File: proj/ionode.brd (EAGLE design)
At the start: 43.2 x 15.2 mm, 34 parts, among them J2 USB-BAMPHENOL-MICRO, U1 ATMEGA1284P-MU44-VQFN, U4 FT232RQFN32, U5 SN74LVC1G125SOT23-5, U6 SN74LVC1G125SOT23-5, U7 3.3V, X1 10MHz

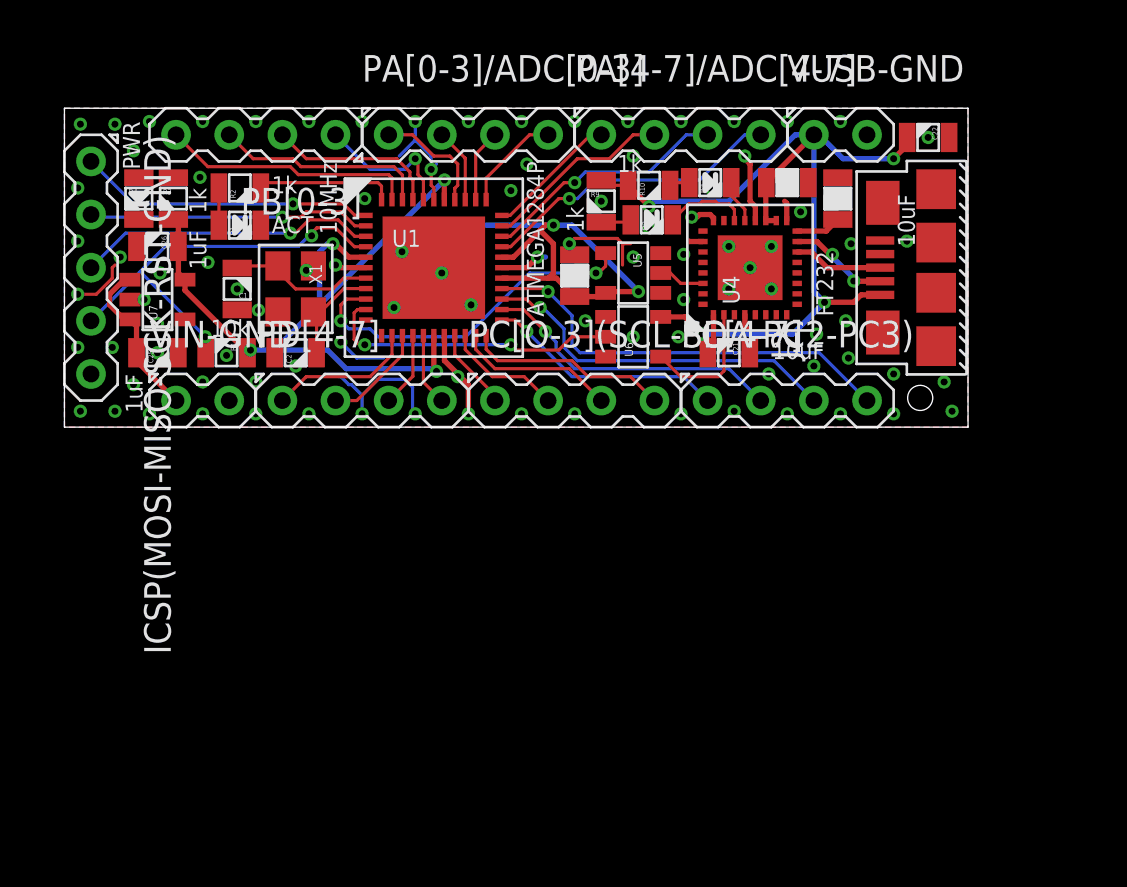
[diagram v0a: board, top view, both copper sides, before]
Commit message: Improved reference designators on ionode
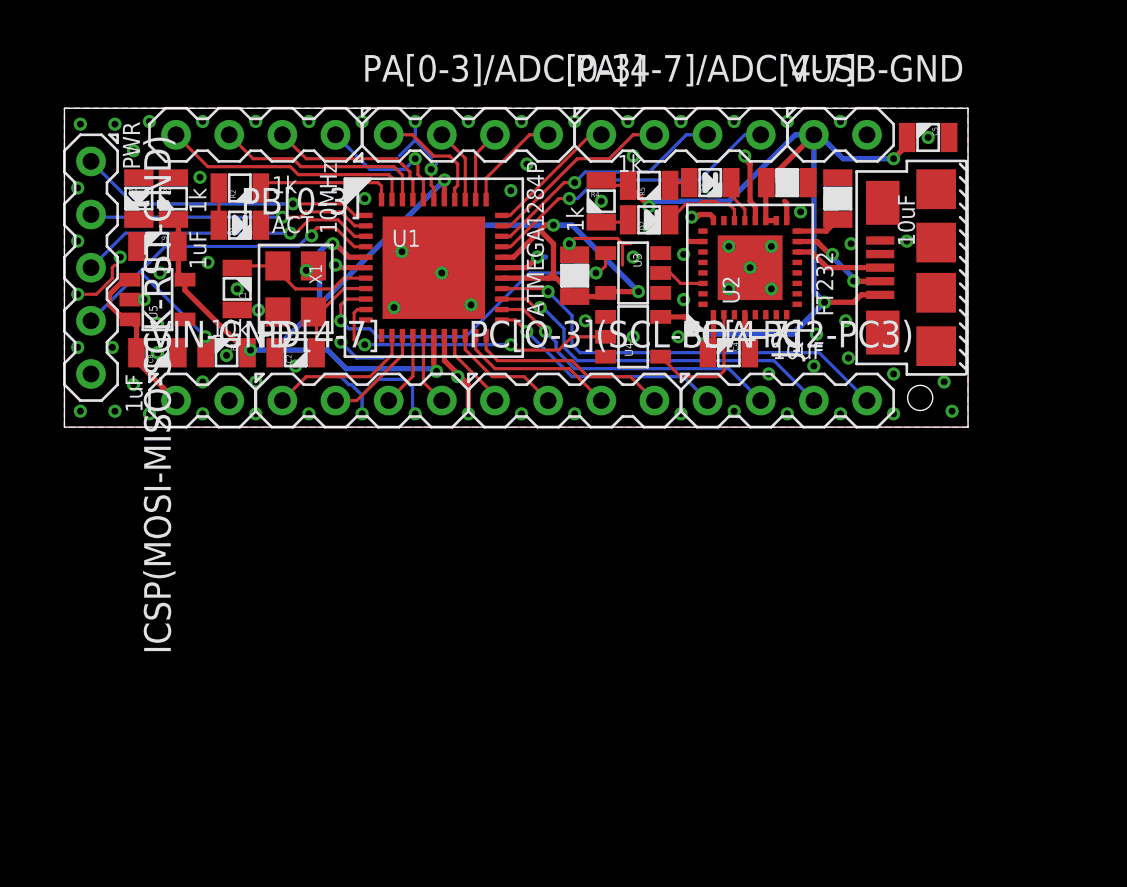
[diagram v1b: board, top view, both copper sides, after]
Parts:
- removed U6: SN74LVC1G125SOT23-5, dooba:SOT23-5
- removed U7: 3.3V, dooba:SOT23-5
- added U2: FT232RQFN32, dooba:32-VQFN
- added U3: SN74LVC1G125SOT23-5, dooba:SOT23-5
- U4: value FT232RQFN32 -> SN74LVC1G125SOT23-5; device dooba:32-VQFN -> dooba:SOT23-5
- U5: value SN74LVC1G125SOT23-5 -> 3.3V
- moved U5 22.8 mm to (28.3, 31.5), turned to 90 degrees
- moved U4 6.49 mm to (51.1, 29.7)
- moved D2 0.13 mm to (51.8, 35.3)
- renumbered C21 to C4, C22 to C5, C23 to C6, C24 to C7, C25 to C8, C26 to C9, R10 to R5, R9 to R4
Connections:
- net 3.3V: now also U3.5; no longer U7.5
- net ATMEGA_RX: now also U3.4; no longer U5.4
- net ATMEGA_TX: now also U4.2; no longer U6.2
- net FT232R_RX: now also U2.P$2, U4.4; no longer U4.P$2, U6.4
- net FT232R_TX: now also U2.P$30, U3.2; no longer U4.P$30, U5.2
- net GND: now also U2.P$17, U2.P$20, U2.P$24, U2.P$26, U2.P$33, U2.P$4, U3.1, U3.3, U4.1, U4.3, U5.2; no longer U4.P$17, U4.P$20, U4.P$24, U4.P$26, U4.P$33, U4.P$4, U5.1, U5.3, U6.1, U6.3, U7.2
- net N$21: now also U2.P$16; no longer U4.P$16
- net N$22: now also U2.P$22; no longer U4.P$22
- net N$23: now also U2.P$21; no longer U4.P$21
- net N$26: now also U2.P$15; no longer U4.P$15
- net N$27: now also U2.P$14; no longer U4.P$14
- net VIN: now also U5.1, U5.3; no longer U7.1, U7.3
- net VUSB: now also U2.P$1, U2.P$18, U2.P$19, U4.5; no longer U4.P$1, U4.P$18, U4.P$19, U6.5
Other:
- board text added: "C1"
- board text added: "C2"
- board text added: "C3"
- board text added: "C4"
- board text added: "C5"
- board text added: "C6"
- board text added: "C7"
- board text added: "C8"
- board text added: "C9"
- board text added: "D1"
- board text added: "D2"
- board text added: "D3"
- board text added: "D4"
- board text added: "J1"
- board text added: "R1"
- board text added: "R2"
- board text added: "R3"
- board text added: "R4"
- board text added: "R5"
- board text added: "U1"
- board text added: "U2"
- board text added: "U3"
- board text added: "U4"
- board text added: "U5"
- board text added: "X1"

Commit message: Added DRU file for ZhongFeng PCBA Added 0402 footprint Added SMD Jumper footprint Added SMD Jumper to ioNode for VIN - VUSB Upgraded most 0805 parts on ioNode to 0402 Added USART1 TX/RX breakout on ioNode Upgraded ioNode board to better use ZFPCBA DRU
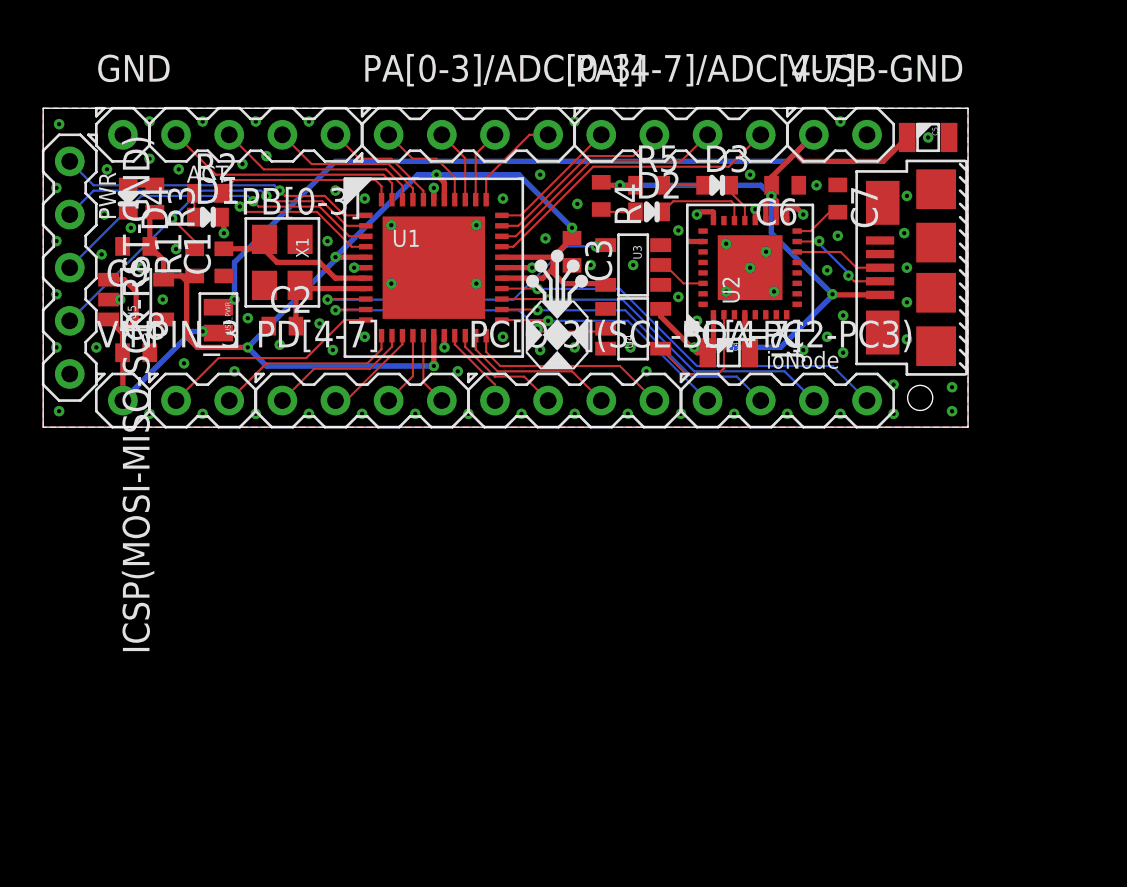
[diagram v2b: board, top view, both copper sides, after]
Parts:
- added GND, VIN: PIN_1, dooba:PIN_1
- added USB_PWR: JMPSMD, dooba:SMD_JMP
- C1, C2, C3, C6, C7, C8, C9, D1, D2, D3, D4, R1, R2, R3, R4, R5: device dooba:0805 -> dooba:0402
- PIN_3: value PIN_2 -> PD[2-3]
- moved R1 4.58 mm to (30.1, 33.3), turned to 90 degrees
- moved D1 1.57 mm to (30.7, 35.4)
- moved R2 1.55 mm to (30.7, 36.6)
- moved C1 1.42 mm to (31.5, 33.3)
- moved X1 1.42 mm to (34.3, 33.3)
- moved C2 1.42 mm to (34.3, 30.2)
- moved C3 1.15 mm to (48.1, 33.8), turned to 270 degrees
- moved C8 1.02 mm to (27.3, 29.0)
- moved C9 1.02 mm to (27.3, 34.0)
- moved ICSP(MOSI-MISO-SCK-RST-GND) 1.02 mm to (24.1, 33.0)
- moved U5 1.02 mm to (27.3, 31.5)
- moved R3 0.89 mm to (28.2, 36.3)
- moved D4 0.51 mm to (26.9, 36.3)
- moved D2 0.38 mm to (51.8, 35.7)
- moved U3 0.38 mm to (51.1, 33.1)
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- renumbered VIN-GND to PIN_3
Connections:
- net GND: now also GND.1; no longer PIN_3.2
- net PD2/RXD1: now also PIN_3.1
- net PD3/TXD1: now also PIN_3.2
- net VIN: now also USB_PWR.2, VIN.1; no longer PIN_3.1
- net VUSB: now also USB_PWR.1
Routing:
- net VUSB: track 46.0 -> 76.2 mm, vias 4 -> 5
- net GND: track 36.0 -> 11.3 mm, vias 97 -> 99
- net PD2/RXD1: track 0.00 -> 10.7 mm
- net PD3/TXD1: track 0.00 -> 8.94 mm
- net 3.3V: track 62.3 -> 55.5 mm, vias 6 -> 5
- net VIN: track 7.82 -> 13.9 mm, vias 0 -> 1
- net N$6: track 6.59 -> 8.68 mm
- net PB7/SCK: track 14.4 -> 16.4 mm
- net PB6/MISO: track 13.6 -> 15.3 mm
- net !RESET: track 20.6 -> 19.3 mm
- net PB0: track 6.82 -> 5.73 mm, vias 1 -> 0
- net N$2: track 7.01 -> 8.03 mm
- net PB5/MOSI: track 14.2 -> 15.2 mm
- net N$25: track 0.97 -> 1.95 mm
- net ATMEGA_RX: track 17.1 -> 16.2 mm
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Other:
- board size 43.2 x 15.2 mm -> 44.2 x 15.2 mm
- board text added: "ioNode"
- board text removed: "10MHz"
- board text removed: "10k"
- board text removed: "10uF"
- board text removed: "1k"
- board text removed: "1uF"
- board text removed: "ATMEGA1284P"
- board text removed: "C1"
- board text removed: "C2"
- board text removed: "C3"
- board text removed: "C6"
- board text removed: "C7"
- board text removed: "C8"
- board text removed: "C9"
- board text removed: "D1"
- board text removed: "D2"
- board text removed: "D3"
- board text removed: "D4"
- board text removed: "FT232"
- board text removed: "R1"
- board text removed: "R2"
- board text removed: "R3"
- board text removed: "R4"
- board text removed: "R5"

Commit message: Completed Tako Module
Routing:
- net GND: track 11.3 -> 13.0 mm
- net VUSB: track 76.2 -> 75.6 mm
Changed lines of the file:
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@@
 <wire x1="38.279" y1="33.02" x2="37.719" y2="33.02" width="0.254" layer="1"/>
 <via x="37.719" y="33.02" extent="1-16" drill="0.2032"/>
-<wire x1="54.392" y1="34.27" x2="53.741" y2="34.27" width="0.254" layer="1"/>
+<wire x1="54.192" y1="34.27" x2="53.741" y2="34.27" width="0.254" layer="1"/>
 <wire x1="53.741" y1="34.27" x2="53.721" y2="34.29" width="0.254" layer="1"/>
-<wire x1="54.892" y1="35.27" x2="54.892" y2="35.659" width="0.254" layer="1"/>
+<wire x1="54.892" y1="35.47" x2="54.892" y2="35.659" width="0.254" layer="1"/>
 <wire x1="54.892" y1="35.659" x2="54.864" y2="35.687" width="0.254" layer="1"/>
 <wire x1="54.864" y1="35.687" x2="54.229" y2="35.687" width="0.254" layer="1"/>
-<wire x1="56.892" y1="35.27" x2="56.892" y2="35.81" width="0.254" layer="1"/>
+<wire x1="56.892" y1="35.47" x2="56.892" y2="35.81" width="0.254" layer="1"/>
 <wire x1="56.892" y1="35.81" x2="56.896" y2="35.814" width="0.254" layer="1"/>
 <via x="56.896" y="35.814" extent="1-16" drill="0.2032"/>
-<wire x1="58.392" y1="35.27" x2="58.392" y2="35.786" width="0.254" layer="1"/>
-<wire x1="56.392" y1="30.77" x2="56.392" y2="30.103" width="0.254" layer="1"/>
+<wire x1="58.392" y1="35.47" x2="58.392" y2="35.786" width="0.254" layer="1"/>
+<wire x1="56.392" y1="30.57" x2="56.392" y2="30.103" width="0.254" layer="1"/>
 <wire x1="56.392" y1="30.103" x2="56.388" y2="30.099" width="0.254" layer="1"/>
 <via x="55.499" y="31.877" extent="1-16" drill="0.2032"/>
@@
 <wire x1="41.529" y1="33.02" x2="40.259" y2="33.02" width="0.254" layer="1"/>
 <wire x1="40.259" y1="33.02" x2="39.497" y2="32.258" width="0.254" layer="1"/>
+<wire x1="53.213" y1="34.798" x2="53.213" y2="34.417" width="0.254" layer="1"/>
+<wire x1="53.213" y1="34.417" x2="53.36" y2="34.27" width="0.254" layer="1"/>
+<wire x1="53.36" y1="34.27" x2="54.192" y2="34.27" width="0.254" layer="1"/>
+<wire x1="56.392" y1="30.103" x2="56.392" y2="29.19" width="0.254" layer="1"/>
+<wire x1="56.392" y1="29.19" x2="56.626" y2="28.956" width="0.254" layer="1"/>
 </signal>
 <signal name="N$21">
 <contactref element="U2" pad="P$16"/>
 <contactref element="C7" pad="2"/>
-<wire x1="58.892" y1="34.77" x2="59.535" y2="34.77" width="0.1016" layer="1"/>
+<wire x1="59.092" y1="34.77" x2="59.535" y2="34.77" width="0.1016" layer="1"/>
 <wire x1="59.535" y1="34.77" x2="60.437" y2="35.672" width="0.1016" layer="1"/>
 <wire x1="60.437" y1="35.672" x2="60.833" y2="35.672" width="0.1016" layer="1"/>
@@
 <contactref element="U2" pad="P$22"/>
 <contactref element="D2" pad="2"/>
-<wire x1="55.892" y1="35.27" x2="55.892" y2="36.056" width="0.1016" layer="1"/>
+<wire x1="55.892" y1="35.47" x2="55.892" y2="36.056" width="0.1016" layer="1"/>
 <wire x1="55.892" y1="36.056" x2="55.753" y2="36.195" width="0.1016" layer="1"/>
 <wire x1="55.753" y1="36.195" x2="52.974" y2="36.195" width="0.1016" layer="1"/>
@@
 <contactref element="U2" pad="P$21"/>
 <contactref element="D3" pad="2"/>
-<wire x1="56.392" y1="35.27" x2="56.392" y2="35.937" width="0.1016" layer="1"/>
+<wire x1="56.392" y1="35.47" x2="56.392" y2="35.937" width="0.1016" layer="1"/>
 <wire x1="56.392" y1="35.937" x2="55.7172" y2="36.6118" width="0.1016" layer="1"/>
 <wire x1="55.7172" y1="36.6118" x2="55.7172" y2="36.957" width="0.1016" layer="1"/>
@@
 <contactref element="J2" pad="2"/>
 <contactref element="U2" pad="P$15"/>
-<wire x1="58.892" y1="34.27" x2="59.924" y2="34.27" width="0.1016" layer="1"/>
+<wire x1="59.092" y1="34.27" x2="59.924" y2="34.27" width="0.1016" layer="1"/>
 <wire x1="59.924" y1="34.27" x2="59.944" y2="34.29" width="0.1016" layer="1"/>
 <via x="59.944" y="34.29" extent="1-16" drill="0.2032"/>
@@
 <contactref element="J2" pad="3"/>
 <contactref element="U2" pad="P$14"/>
-<wire x1="58.892" y1="33.77" x2="60.972" y2="33.77" width="0.1016" layer="1"/>
+<wire x1="59.092" y1="33.77" x2="60.972" y2="33.77" width="0.1016" layer="1"/>
 <wire x1="60.972" y1="33.77" x2="61.722" y2="33.02" width="0.1016" layer="1"/>
 <wire x1="61.722" y1="33.02" x2="62.857" y2="33.02" width="0.1016" layer="1"/>
@@
 <contactref element="U2" pad="P$30"/>
 <contactref element="U3" pad="2"/>
-<wire x1="54.392" y1="32.27" x2="53.455" y2="32.27" width="0.1016" layer="1"/>
+<wire x1="54.192" y1="32.27" x2="53.455" y2="32.27" width="0.1016" layer="1"/>
 <wire x1="53.455" y1="32.27" x2="52.832" y2="32.893" width="0.1016" layer="1"/>
 <wire x1="52.832" y1="32.893" x2="52.623" y2="32.893" width="0.1016" layer="1"/>
@@
 <contactref element="U2" pad="P$2"/>
 <contactref element="U4" pad="4"/>
-<wire x1="55.392" y1="30.77" x2="55.392" y2="28.214" width="0.1016" layer="1"/>
+<wire x1="55.392" y1="30.57" x2="55.392" y2="28.214" width="0.1016" layer="1"/>
 <wire x1="55.392" y1="28.214" x2="55.118" y2="27.94" width="0.1016" layer="1"/>
 <wire x1="55.118" y1="27.94" x2="53.578" y2="27.94" width="0.1016" layer="1"/>
@@
 <wire x1="63.008" y1="38.1" x2="59.182" y2="38.1" width="0.254" layer="1"/>
 <wire x1="59.182" y1="38.1" x2="58.801" y2="38.481" width="0.254" layer="1"/>
-<wire x1="57.392" y1="35.27" x2="57.392" y2="36.183" width="0.254" layer="1"/>
+<wire x1="57.392" y1="35.47" x2="57.392" y2="36.183" width="0.254" layer="1"/>
 <wire x1="57.392" y1="36.183" x2="57.658" y2="36.449" width="0.254" layer="1"/>
-<wire x1="57.892" y1="35.27" x2="57.892" y2="36.215" width="0.254" layer="1"/>
+<wire x1="57.892" y1="35.47" x2="57.892" y2="36.215" width="0.254" layer="1"/>
 <wire x1="57.892" y1="36.215" x2="57.658" y2="36.449" width="0.254" layer="1"/>
-<wire x1="54.892" y1="30.77" x2="54.892" y2="29.222" width="0.254" layer="1"/>
+<wire x1="54.892" y1="30.57" x2="54.892" y2="29.222" width="0.254" layer="1"/>
 <wire x1="54.892" y1="29.222" x2="54.626" y2="28.956" width="0.254" layer="1"/>
 <wire x1="52.369" y1="31.049" x2="52.369" y2="30.689" width="0.254" layer="1"/>
